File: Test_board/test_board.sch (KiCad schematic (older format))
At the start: 16 parts, among them J1 CONN_02X26, J2 CONN_02X26

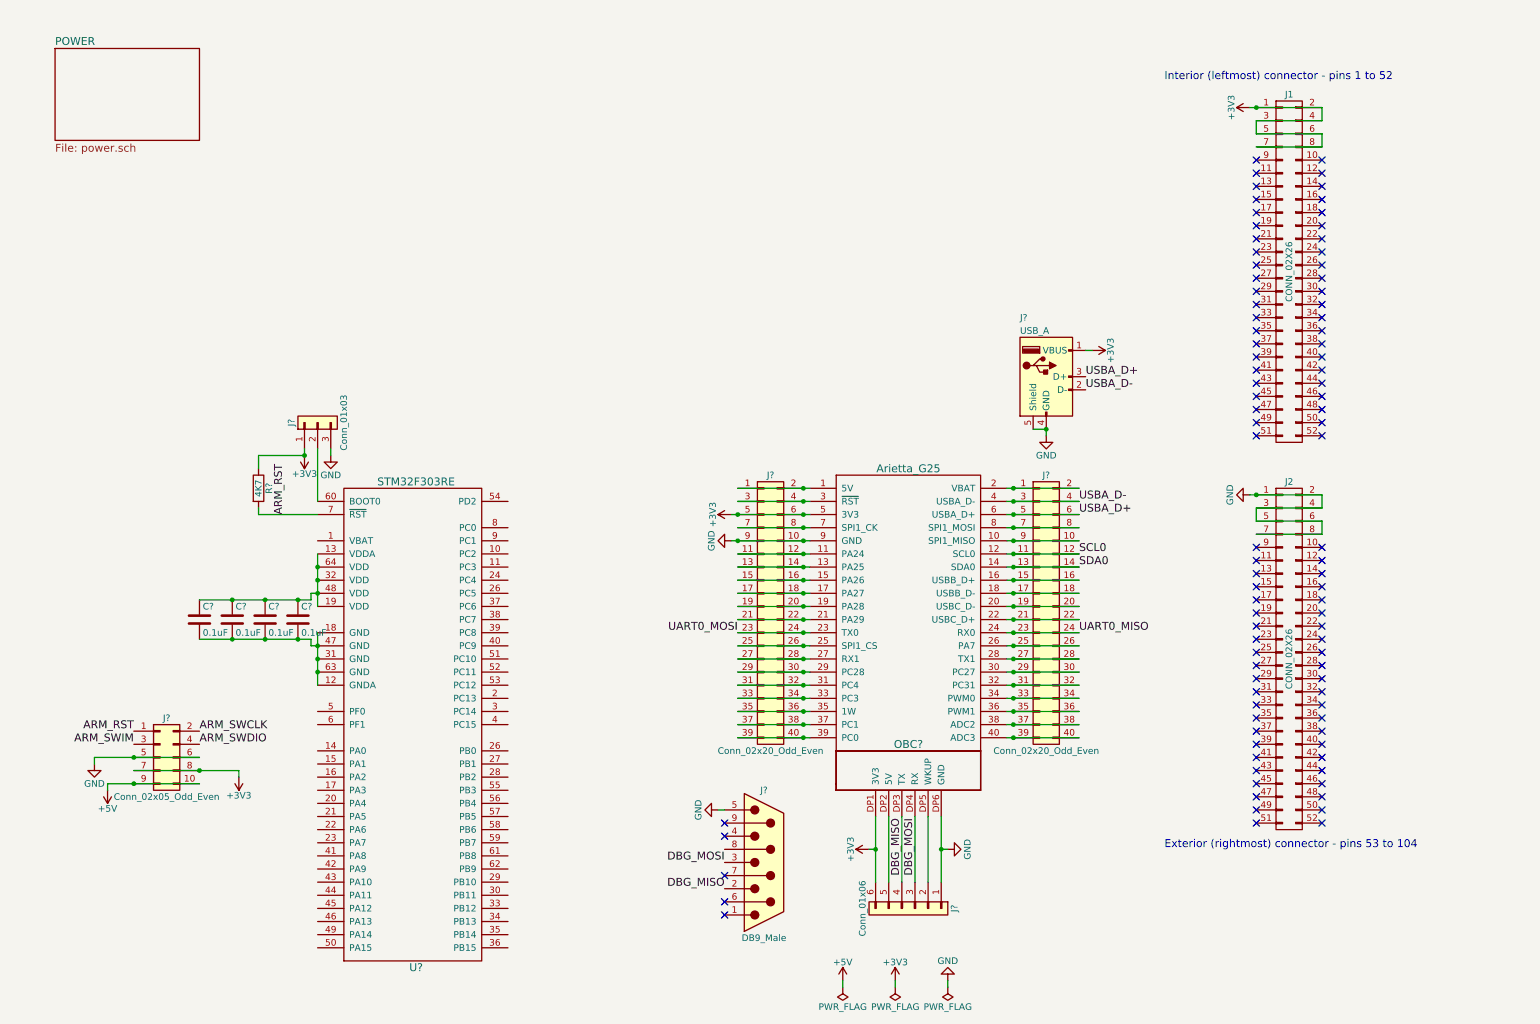
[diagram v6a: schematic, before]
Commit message: Added temp, rtc, and mcu connections
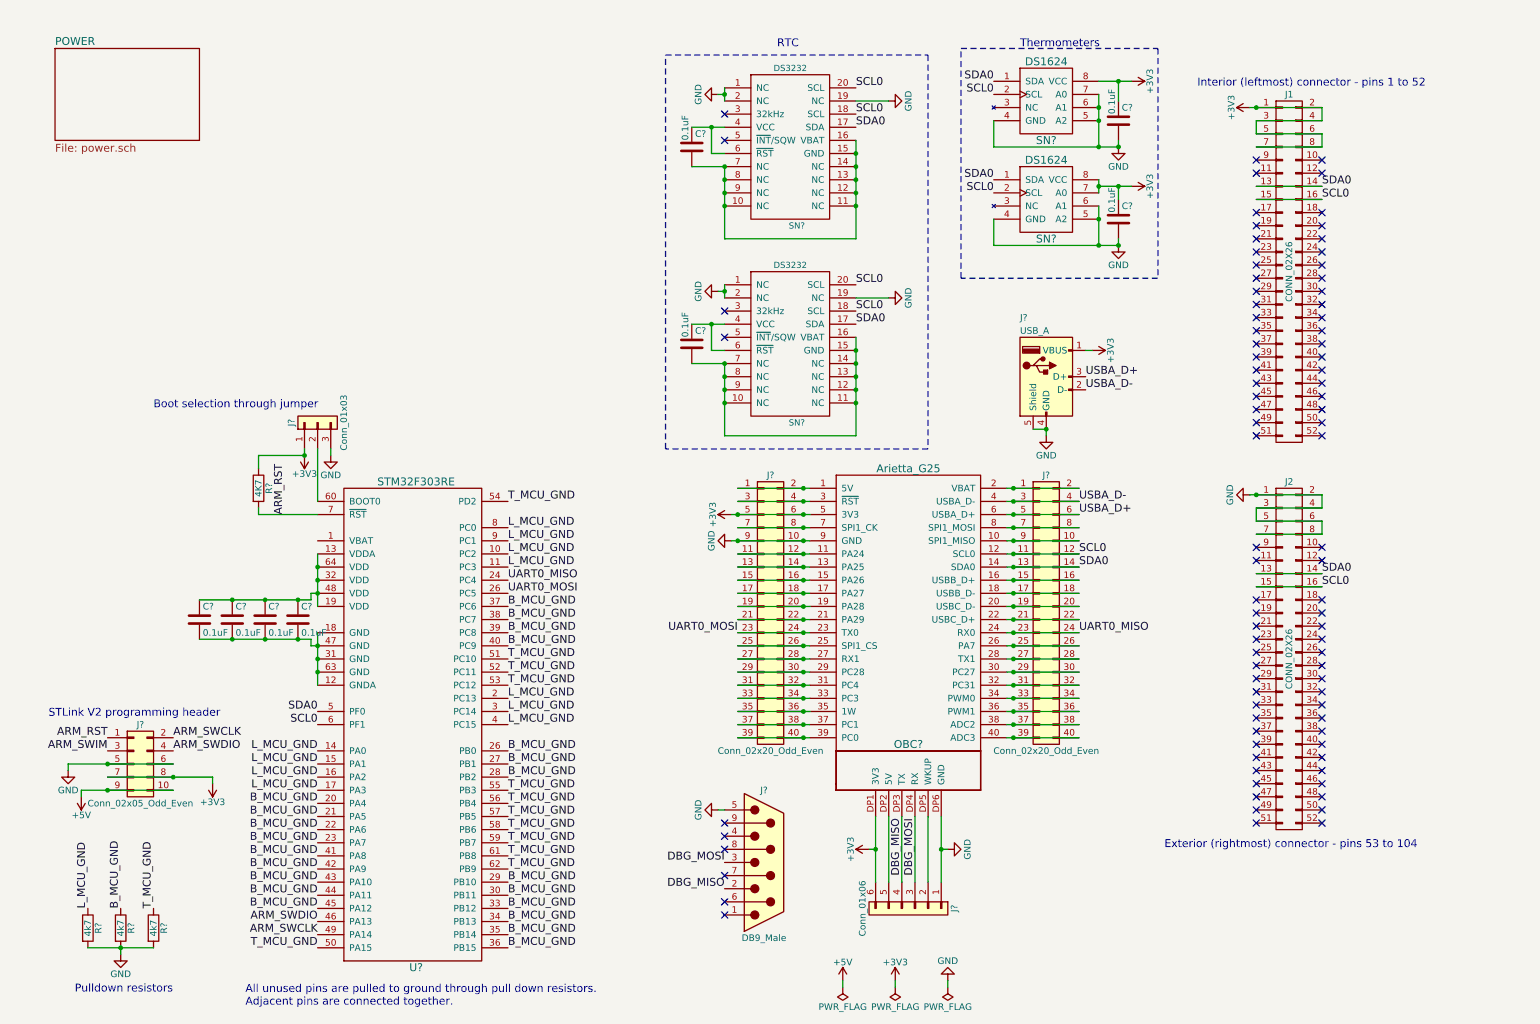
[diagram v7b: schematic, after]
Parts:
- added C? (x4): 0.1uF, 0805, symbol C
- added R? (x3): 4k7, 0805, symbol R
- added SN? (x2): DS1624, symbol DS1624
- added SN? (x2): DS3232, symbol DS3232
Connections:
- net +3V3: now also C?.1, C?.1, SN?.7 (A0), SN?.8 (VCC), SN?.8 (VCC)
- net ARM_SWCLK: now also U?.49 (PA14)
- net ARM_SWDIO: now also U?.46 (PA13)
- net GND: now also C?.2, C?.2, R?.2, R?.2, R?.2, SN?.1 (NC), SN?.1 (NC), SN?.19 (NC), SN?.19 (NC), SN?.2 (NC), SN?.2 (NC), SN?.4 (GND), SN?.4 (GND), SN?.5 (A2), SN?.5 (A2), SN?.6 (A1), SN?.6 (A1), SN?.7 (A0)
- net SCL0: now also J1.15 (P15), J1.16 (P16), J2.15 (P15), J2.16 (P16), U?.6 (PF1), SN?.18 (SCL), SN?.18 (SCL), SN?.2 (SCL), SN?.2 (SCL), SN?.20 (SCL), SN?.20 (SCL)
- net SDA0: now also J1.13 (P13), J1.14 (P14), J2.13 (P13), J2.14 (P14), U?.5 (PF0), SN?.1 (SDA), SN?.1 (SDA), SN?.17 (SDA), SN?.17 (SDA)
- net UART0_MISO: now also U?.24 (PC4)
- net UART0_MOSI: now also U?.26 (PC5)
- net L_MCU_GND: now reaches U?.10 (PC2)
- net L_MCU_GND: now also U?.11 (PC3), U?.14 (PA0), U?.15 (PA1), U?.16 (PA2), U?.17 (PA3), U?.2 (PC13), U?.3 (PC14), U?.4 (PC15), U?.8 (PC0), U?.9 (PC1), R?.1
- net B_MCU_GND: now reaches U?.20 (PA4)
- net B_MCU_GND: now also U?.21 (PA5), U?.22 (PA6), U?.23 (PA7), U?.26 (PC5), U?.27 (PB1), U?.28 (PB2), U?.29 (PB10), U?.30 (PB11), U?.33 (PB12), U?.34 (PB13), U?.35 (PB14), U?.36 (PB15), U?.37 (PC6), U?.38 (PC7), U?.39 (PC8), U?.40 (PC9), U?.41 (PA8), U?.42 (PA9), U?.43 (PA10), U?.44 (PA11), U?.45 (PA12), R?.1
- net T_MCU_GND: now reaches U?.50 (PA15)
- net T_MCU_GND: now also U?.51 (PC10), U?.52 (PC11), U?.53 (PC12), U?.54 (PD2), U?.55 (PB3), U?.56 (PB4), U?.57 (PB5), U?.58 (PB6), U?.59 (PB7), U?.61 (PB8), U?.62 (PB9), R?.1
- new net: C?.2, SN?.10 (NC), SN?.11 (NC), SN?.12 (NC), SN?.13 (NC), SN?.14 (NC), SN?.15 (GND), SN?.16 (VBAT), SN?.7 (NC), SN?.8 (NC), SN?.9 (NC) (x2)
- new net: C?.1, SN?.4 (VCC), SN?.6 (~RST) (x2)
- no-connect marks 93 -> 90
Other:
- note added: "All unused pins are pulled to ground through pull down resistors.\nAdjacent pins are connected together."
- note added: "Boot selection through jumper"
- note added: "Pulldown resistors"
- note added: "RTC"
- note added: "STLink V2 programming header"
- note added: "Thermometers"
- moved on the sheet: J?

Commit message: Wired the whole first sheet
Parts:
- removed C?: 0.1uF, 0805, symbol C
- removed SN?: DS3232, symbol DS3232
- added C6: 0.1uF, 0805, symbol C
- added Q?: Q_NMOS_GSD, symbol Q_NMOS_GSD
- added R? (x2): 1k, 0805, symbol R
- added U2: 24LC256, Housings_SOIC:SOIC-8_3.9x4.9mm_Pitch1.27mm, symbol 24LC256
- added U?: MAX6730A, symbol MAX6730A
- gave numbers to parts that had none: 23
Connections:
- net +3V3: now also C6.1, R?.2, R?.2, U2.8 (VCC), U?.4 (~MR), U?.6 (VCC)
- net ARM_RST: now also Q?.3 (D)
- net GND: now also J2.45 (P45), J2.46 (P46), J2.47 (P47), J2.48 (P48), J2.49 (P49), J2.50 (P50), J2.51 (P51), J2.52 (P52), C6.2, U2.1 (A0), U2.2 (A1), U2.3 (A2), U2.4 (GND), U?.2 (GND)
- net SCL0: now also R?.1, U2.6 (SCL)
- net SDA0: now also R?.1, U2.5 (SDA)
- net +BATT: now reaches J1.45 (P45)
- net +BATT: now also J1.46 (P46), J1.47 (P47), J1.48 (P48), J1.49 (P49), J1.50 (P50), J1.51 (P51), J1.52 (P52)
- net WDT_KICK: now reaches J5.15 (Pin_15), J5.16 (Pin_16), OBC1.15 (PA26)
- net WDT_KICK: now also U?.5 (WDI)
- net USB_D-: now reaches J8.19 (Pin_19), J8.20 (Pin_20), OBC1.20 (USBC_D-)
- net USB_D-: now also J9.2 (D-)
- net USB_D+: now reaches J8.21 (Pin_21), J8.22 (Pin_22), OBC1.22 (USBC_D+)
- net USB_D+: now also J9.3 (D+)
- net ~OBC_RST: now reaches J5.3 (Pin_3), J5.4 (Pin_4), OBC1.3 (~RST)
- net ~OBC_RST: now also U?.1 (~RST)
- net ARM_MSTR_RST: now reaches J5.33 (Pin_33), J5.34 (Pin_34), OBC1.33 (PC3)
- net ARM_MSTR_RST: now also Q?.1 (G)
- net EEPROM_WP: now reaches J5.39 (Pin_39), J5.40 (Pin_40), OBC1.39 (PC0)
- net EEPROM_WP: now also U2.7 (WP)
- net at C1.2, C2.2, C3.2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: now also Q?.2 (S)
- net USBA_D+: no longer names the net of J8.5 (Pin_5), J8.6 (Pin_6), OBC1.6 (USBA_D+)
- net USBA_D+: no longer J9.3 (D+)
- net USBA_D-: no longer names the net of J8.3 (Pin_3), J8.4 (Pin_4), OBC1.4 (USBA_D-)
- net USBA_D-: no longer J9.2 (D-)
- no-connect marks 90 -> 73
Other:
- note added: "256kB EEPROM in socket"
- note added: "I2C pullups"
- note added: "Watchdog Timer"
